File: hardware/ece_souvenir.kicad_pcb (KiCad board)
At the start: 2 copper layers, 30 x 30 mm, 38 parts, among them U1 TLC555CDR

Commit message: feat(pcb): switch to 0603 hand-solder parts and re-place
All parts will be hand soldered, so nothing smaller than 0603: LEDs
XL-1608UOC-06 (C965800), passives 0603 with KiCad HandSolder footprints.
C1 back to X7R (Yageo C106248) per the original spec now that JLC
basic/extended fees no longer apply. Series resistors moved inside each
digit to fit the larger 0603 courtyards.

ERC 0, netlist OK. DRC: 0 violations, 0 parity, 57 unconnected (routing
pending).

Co-Authored-By: Claude Opus 5.5 <noreply@anthropic.com>
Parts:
- C1, C2, C3: footprint Capacitor_SMD:C_0402_1005Metric -> Capacitor_SMD:C_0603_1608Metric_Pad1.08x0.95mm_HandSolder
- D1, D10, D11, D12, D13, D14, D2, D3, D4, D5, D6, D7, D8, D9: footprint LED_SMD:LED_0402_1005Metric -> LED_SMD:LED_0603_1608Metric_Pad1.05x0.95mm_HandSolder
- R1, R10, R11, R12, R13, R14, R15, R16, R2, R3, R4, R5, R6, R7, R8, R9: footprint Resistor_SMD:R_0402_1005Metric -> Resistor_SMD:R_0603_1608Metric_Pad0.98x0.95mm_HandSolder
- moved C1 1.55 mm to (18.4, 25.8)
- moved R8 1.21 mm to (13.6, 5.50)
- moved R11 1.21 mm to (13.6, 12.5)
- moved R3 1.21 mm to (21.6, 5.50)
- moved R5 1.21 mm to (21.6, 7.50)
- moved R7 1.21 mm to (21.6, 12.5)
- moved R12 1.21 mm to (5.58, 5.50)
- moved R14 1.21 mm to (5.58, 7.50)
- moved R16 1.21 mm to (5.58, 12.5)
- moved R1 1.14 mm to (11.4, 25.4)
- moved C3 0.89 mm to (19.6, 22.6)
- moved R10 0.54 mm to (16.0, 11.5)
- moved R15 0.54 mm to (8.00, 11.5)
- moved R6 0.54 mm to (24.0, 11.5)
- moved R13 0.54 mm to (8.00, 6.50)
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
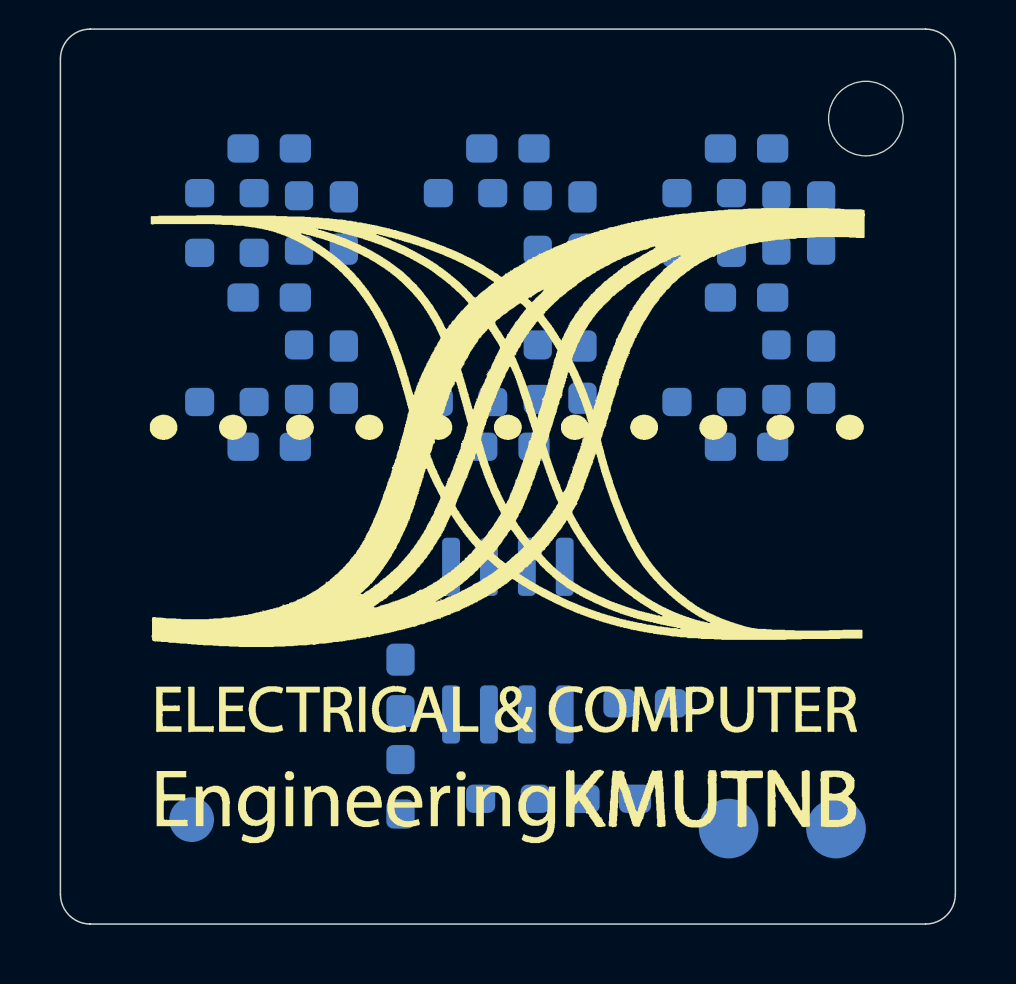
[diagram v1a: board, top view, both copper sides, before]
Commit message: feat(pcb): standalone LEDs, series resistors in a row below digits
Per request, LEDs stand alone in the digit area. R3-R16 move to a single
row of vertical 0603s at y=17.6 (bottom view), grouped per digit; U1 and
timing parts shift down to the bottom edge.

DRC: 0 violations, 0 parity, 57 unconnected (routing next).

Co-Authored-By: Claude Opus 5.5 <noreply@anthropic.com>
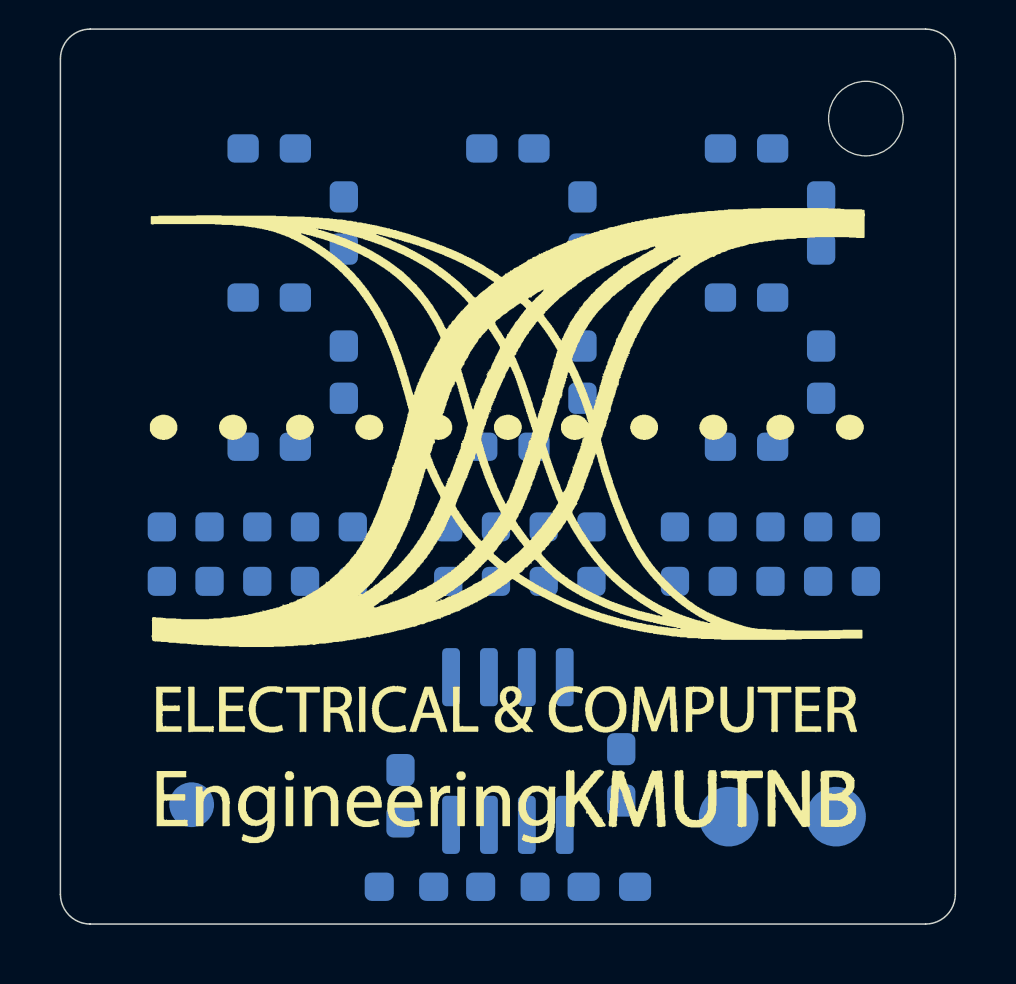
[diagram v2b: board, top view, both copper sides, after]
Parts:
- moved R3 12.3 mm to (23.8, 17.6), turned to 90 degrees
- moved R12 12.1 mm to (6.60, 17.6), turned to 90 degrees
- moved R8 12.1 mm to (14.6, 17.6), turned to 90 degrees
- moved R4 11.5 mm to (27.0, 17.6)
- moved R13 11.2 mm to (9.80, 17.6)
- moved R9 11.2 mm to (17.8, 17.6)
- moved R5 10.1 mm to (22.2, 17.6), turned to 90 degrees
- moved R14 10.1 mm to (5.00, 17.6), turned to 90 degrees
- moved R6 6.26 mm to (25.4, 17.6)
- moved R10 6.10 mm to (16.2, 17.6)
- moved R15 6.10 mm to (8.20, 17.6)
- moved R16 5.55 mm to (3.40, 17.6), turned to 90 degrees
- moved R7 5.19 mm to (20.6, 17.6), turned to 90 degrees
- moved R11 5.13 mm to (13.0, 17.6), turned to 90 degrees
- moved C2 3.70 mm to (11.4, 25.7)
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
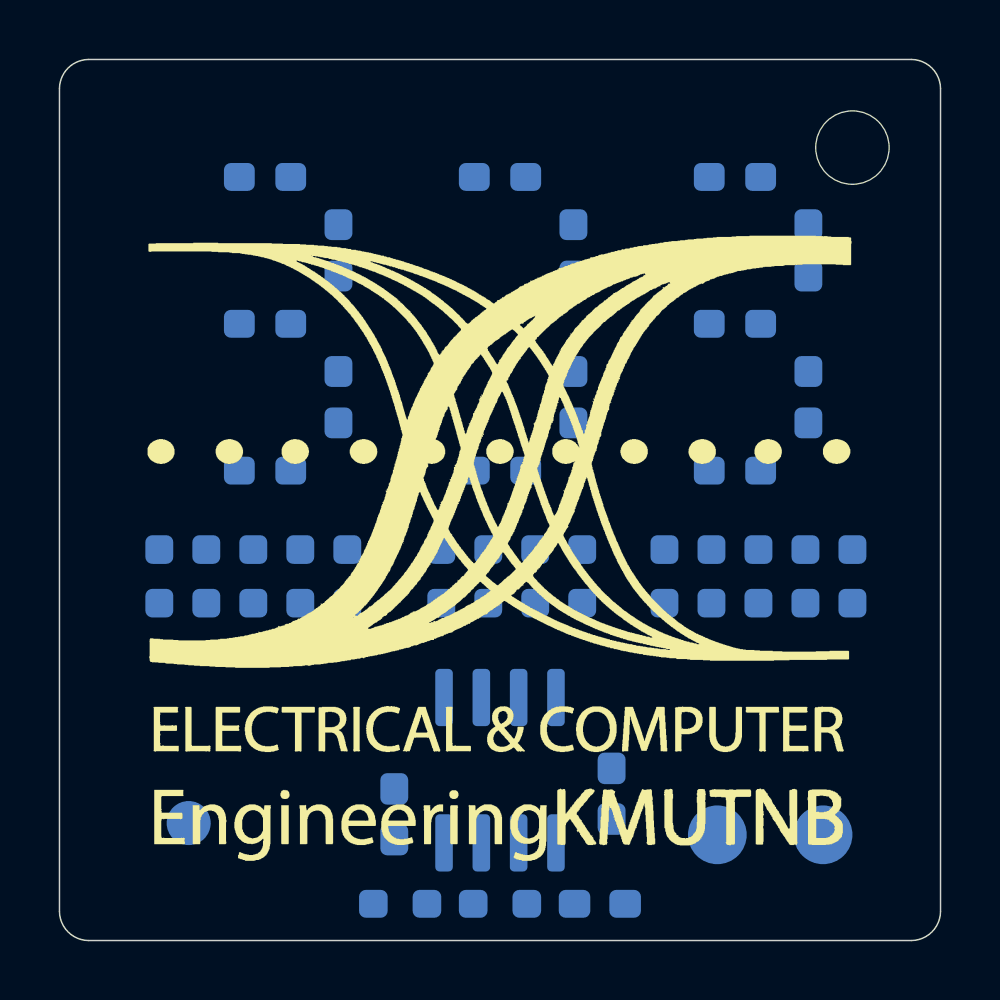
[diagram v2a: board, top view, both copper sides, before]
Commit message: feat(pcb): autoroute via Konnect + Freerouting, DRC clean
KiCad native DSN export (bottom-side parts, roundrect pads and arc
corners are outside Konnect's own Specctra profile) -> Konnect
route_specctra_dsn (local Freerouting 2.4.1, JRE 25) -> KiCad SES import.
DSN boundary inset 0.1 mm for the 0.3 mm edge rule; top-layer traces
weighted 4-6x so the logo side carries only crossings. Freerouting
neck-downs (0.15 mm) widened back to net-class width.

Result: 267 mm B.Cu, 59.5 mm F.Cu, 14 tented vias.
DRC: 0 violations, 0 unconnected, 0 schematic parity issues.

Co-Authored-By: Claude Opus 5.5 <noreply@anthropic.com>
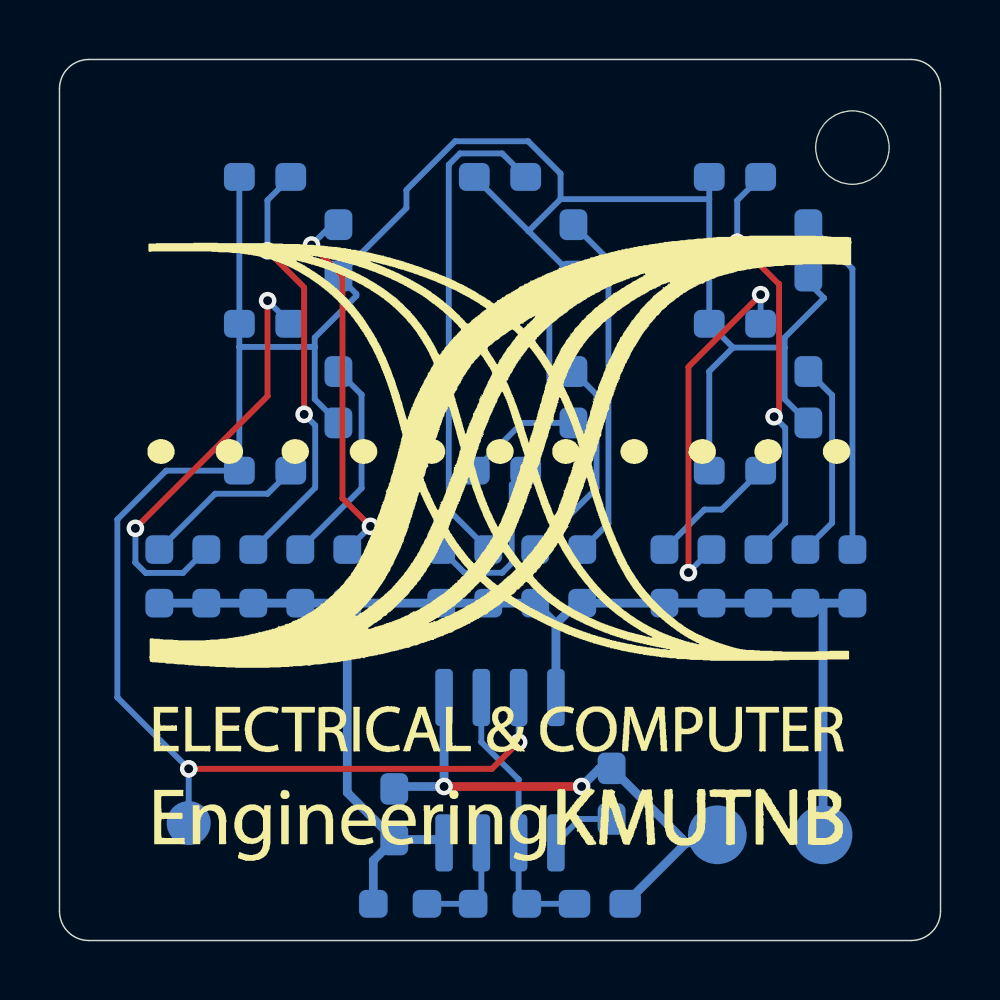
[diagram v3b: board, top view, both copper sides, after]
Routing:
- net /LED_SINK: track 0.00 -> 98.5 mm, vias 0 -> 2
- net VCC: track 0.00 -> 47.5 mm
- net GND: track 0.00 -> 18.4 mm, vias 0 -> 2
- net Net-(D6-A): track 0.00 -> 16.8 mm
- net Net-(D12-A): track 0.00 -> 14.8 mm, vias 0 -> 2
- net Net-(D10-A): track 0.00 -> 14.6 mm, vias 0 -> 2
- net Net-(D1-A): track 0.00 -> 14.2 mm, vias 0 -> 2
- net Net-(D11-A): track 0.00 -> 12.7 mm, vias 0 -> 2
- net Net-(D3-A): track 0.00 -> 12.6 mm, vias 0 -> 2
- net Net-(D7-A): track 0.00 -> 11.9 mm
- net Net-(D2-A): track 0.00 -> 11.7 mm
- net /TH: track 0.00 -> 9.29 mm
- net Net-(D13-A): track 0.00 -> 7.25 mm
- net Net-(D8-A): track 0.00 -> 7.25 mm
- net Net-(D4-A): track 0.00 -> 6.77 mm
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
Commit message: feat(pcb): single-sided routing, logo side copper-free
All 334.9 mm of track on B.Cu with the parts: no F.Cu traces, no vias,
so the top shows only the logo on white mask.

- LED polarity 180 deg (a/g/d) / 270 deg (f/e) instead of spec 0/90:
  same look, but all cathodes meet at each digit's inner-left corner so
  sink and anode paths nest without crossing on one layer.
- Resistor row reordered f e d g a per digit to match.
- Router: F.Cu inactive, vias off, keepouts between LED/resistor pads
  (hand-solder bridge safety); route.py reports any between-pad
  crossing (0 on this board). Freerouting 2.4.1 drops the netlist if a
  keepout precedes autoroute_settings, so settings go first.

DRC: 0 violations, 0 unconnected, 0 schematic parity issues.

Co-Authored-By: Claude Opus 5.5 <noreply@anthropic.com>
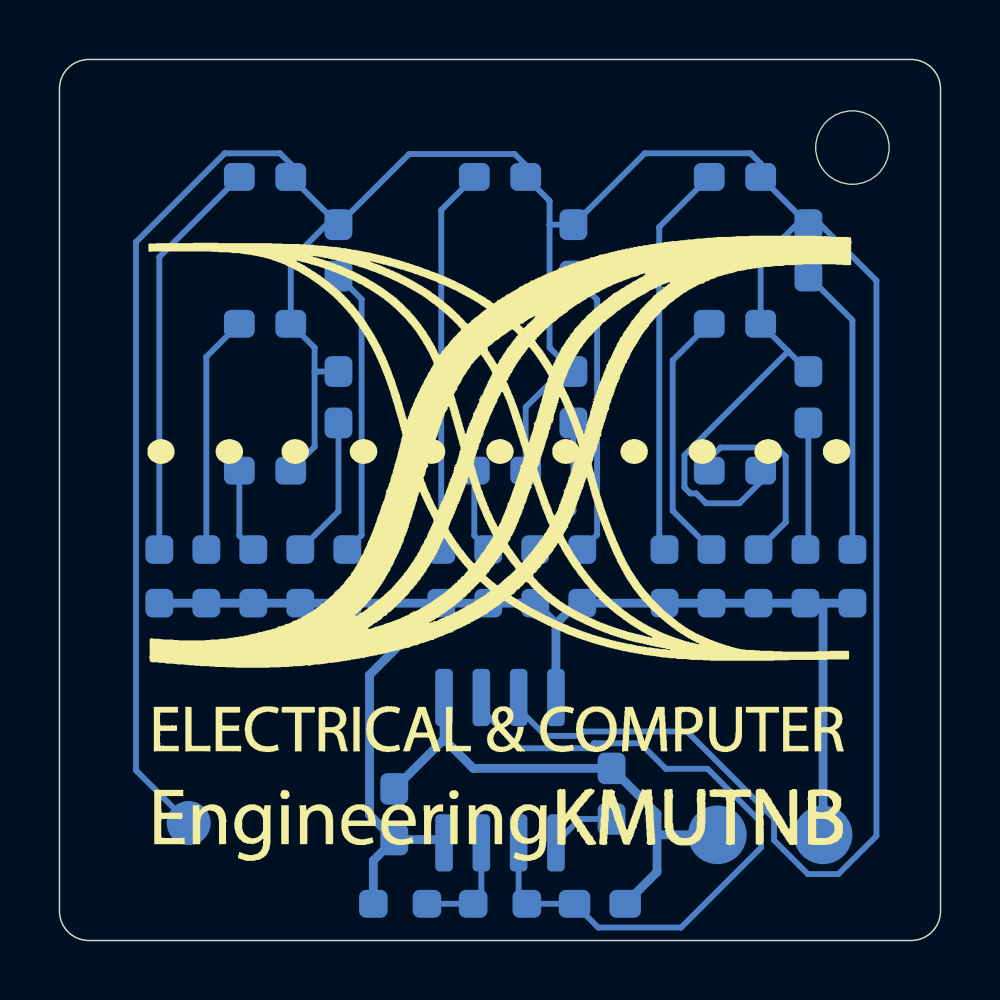
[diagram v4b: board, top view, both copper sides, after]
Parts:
- moved R12 3.20 mm to (3.40, 17.6)
- moved R16 3.20 mm to (6.60, 17.6)
- moved R3 3.20 mm to (20.6, 17.6)
- moved R7 3.20 mm to (23.8, 17.6)
- moved R11 1.60 mm to (14.6, 17.6)
- moved R8 1.60 mm to (13.0, 17.6)
- turned D1 to 180 degrees
- turned D10 to 180 degrees
- turned D11 to -90 degrees
- turned D12 to 180 degrees
- turned D13 to -90 degrees
- turned D14 to 180 degrees
- turned D2 to -90 degrees
- turned D3 to 180 degrees
- turned D4 to -90 degrees
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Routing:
- net /LED_SINK: track 98.5 -> 125.2 mm, vias 2 -> 0
- net /TH: track 9.29 -> 24.2 mm
- net Net-(D12-A): track 14.8 -> 8.15 mm, vias 2 -> 0
- net Net-(D3-A): track 12.6 -> 8.75 mm, vias 2 -> 0
- net Net-(D6-A): track 16.8 -> 13.2 mm
- net Net-(D9-A): track 6.21 -> 2.88 mm
- net Net-(D11-A): track 12.7 -> 9.84 mm, vias 2 -> 0
- net Net-(D14-A): track 5.59 -> 2.88 mm
- net Net-(D5-A): track 4.39 -> 6.85 mm
- net Net-(D4-A): track 6.77 -> 4.35 mm
- net Net-(D13-A): track 7.25 -> 4.85 mm
- net Net-(D8-A): track 7.25 -> 4.85 mm
- net Net-(D7-A): track 11.9 -> 9.86 mm
- net Net-(D2-A): track 11.7 -> 9.93 mm
- net Net-(D1-A): track 14.2 -> 13.5 mm, vias 2 -> 0
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
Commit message: chore(pcb): board moved onto drawing sheet in KiCad (user edit)
Whole board translated by (+111.1825, +56.0585) mm; no other change
(148 segments, 38 footprints, identical relative geometry).

Co-Authored-By: Claude Opus 5.5 <noreply@anthropic.com>
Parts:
- moved C1 124.5 mm to (129.6, 84.8)
- moved D1 124.5 mm to (134.2, 60.1)
- moved D10 124.5 mm to (118.2, 60.1)
- moved D11 124.5 mm to (120.7, 62.6)
- moved D12 124.5 mm to (118.2, 65.1)
- moved D13 124.5 mm to (120.7, 67.6)
- moved D14 124.5 mm to (118.2, 70.1)
- moved D2 124.5 mm to (136.7, 62.6)
- moved D3 124.5 mm to (134.2, 65.1)
- moved D4 124.5 mm to (136.7, 67.6)
- moved D5 124.5 mm to (134.2, 70.1)
- moved D6 124.5 mm to (126.2, 60.1)
- moved D7 124.5 mm to (128.7, 62.6)
- moved D8 124.5 mm to (128.7, 67.6)
- moved D9 124.5 mm to (126.2, 70.1)
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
